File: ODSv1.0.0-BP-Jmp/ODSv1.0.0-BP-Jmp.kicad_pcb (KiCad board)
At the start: 2 copper layers, 150 x 150 mm, 73 parts, among them J1 Conn_01x16, J10 Conn_02x10_Odd_Even, J11 Conn_02x10_Odd_Even, J12 Conn_02x10_Odd_Even, J13 Conn_02x10_Odd_Even, J14 Conn_02x10_Odd_Even, J15 Conn_02x10_Odd_Even, J16 Conn_02x10_Odd_Even, J17 Conn_02x10_Odd_Even, J18 Conn_02x10_Odd_Even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

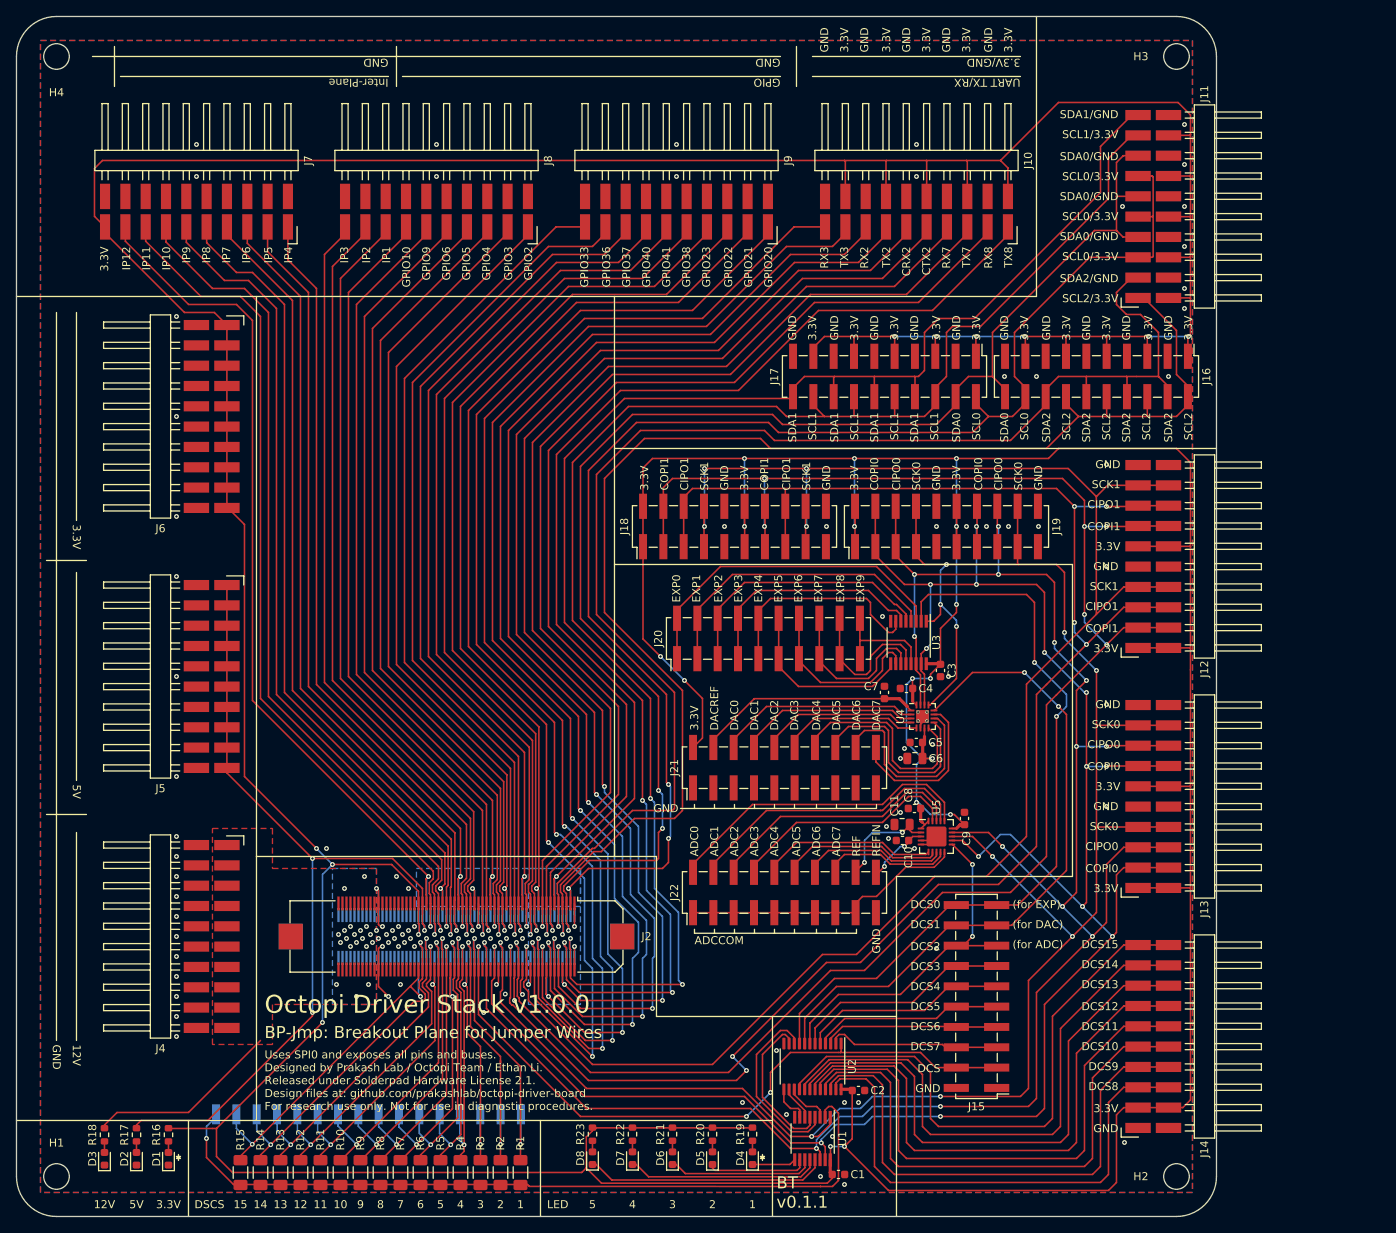
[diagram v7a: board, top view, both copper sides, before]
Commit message: Add silkscreen labels showing BP-Jmp's various sections
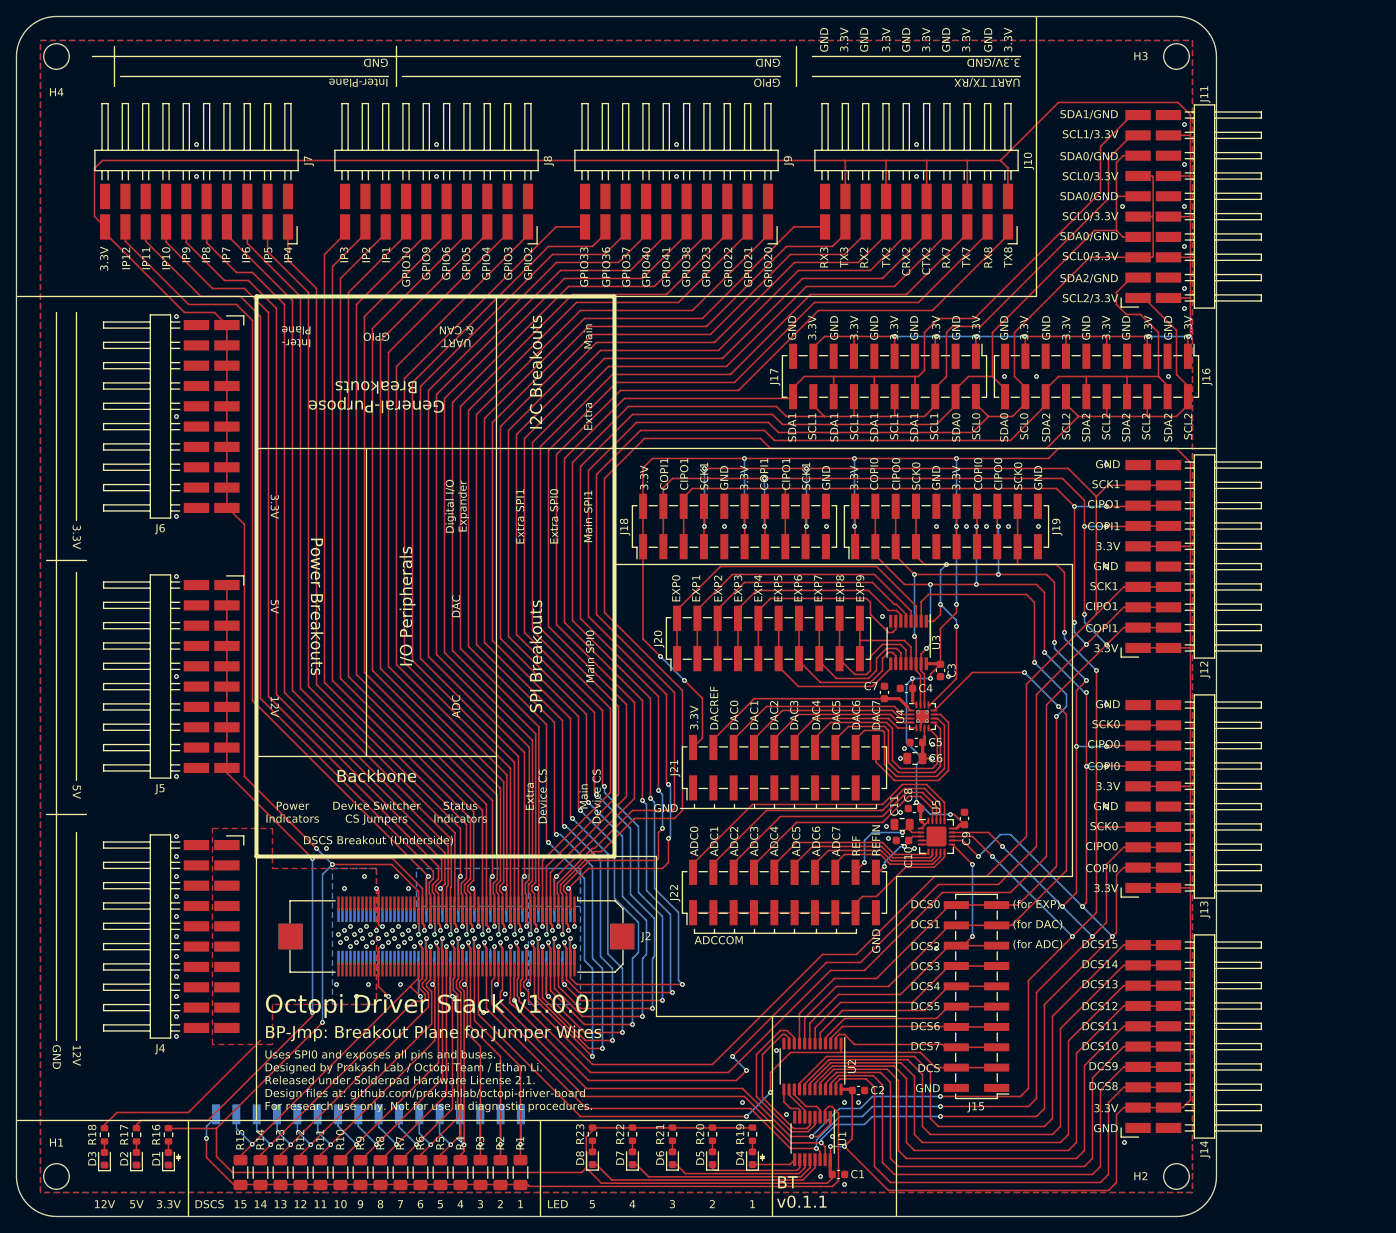
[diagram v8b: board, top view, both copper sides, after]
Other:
- board text added: "ADC"
- board text added: "Backbone"
- board text added: "DAC"
- board text added: "DSCS Breakout (Underside)"
- board text added: "Device Switcher CS Jumpers"
- board text added: "Digital I/O Expander"
- board text added: "Extra"
- board text added: "Extra Device CS"
- board text added: "Extra SPI0"
- board text added: "Extra SPI1"
- board text added: "General-Purpose Breakouts"
- board text added: "I/O Peripherals"
- board text added: "I2C Breakouts"
- board text added: "Inter- Plane"
- board text added: "Main"
- board text added: "Main Device CS"
- board text added: "Main SPI0"
- board text added: "Main SPI1"
- board text added: "Power Breakouts"
- board text added: "Power Indicators"
- board text added: "SPI Breakouts"
- board text added: "Status Indicators"
- board text added: "UART & CAN"
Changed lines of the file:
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@@
   (general
     (thickness 1.6)
-    (drawings 342)
+    (drawings 375)
     (tracks 2545)
     (zones 0)
@@
   )
   (layers
-    (0 F.Cu signal)
-    (31 B.Cu signal)
+    (0 F.Cu signal hide)
+    (31 B.Cu signal hide)
     (32 B.Adhes user)
     (33 F.Adhes user)
@@
     )
   )
+  (gr_text "DSCS Breakout (Underside)" (at 75.25 163) (layer F.SilkS)
+    (effects (font (size 1 1) (thickness 0.15)))
+  )
+  (gr_text "Extra\nDevice CS" (at 95 157.5 90) (layer F.SilkS)
+    (effects (font (size 1 1) (thickness 0.15)))
+  )
+  (gr_text "Main\nDevice CS" (at 101.75 157.5 90) (layer F.SilkS)
+    (effects (font (size 1 1) (thickness 0.15)))
+  )
+  (gr_line (start 30 95) (end 60 95) (layer F.SilkS) (width 0.12))
+  (gr_line (start 60 95) (end 104.75 95) (layer F.SilkS) (width 0.5))
+  (gr_line (start 60 95) (end 60 165) (layer F.SilkS) (width 0.5))
+  (gr_line (start 60 165) (end 104.75 165) (layer F.SilkS) (width 0.5))
+  (gr_text "Extra SPI1" (at 93 122.5 90) (layer F.SilkS)
+    (effects (font (size 1 1) (thickness 0.15)))
+  )
+  (gr_text "Extra SPI0" (at 97.25 122.5 90) (layer F.SilkS)
+    (effects (font (size 1 1) (thickness 0.15)))
+  )
+  (gr_text "Main SPI0" (at 101.75 140 90) (layer F.SilkS)
+    (effects (font (size 1 1) (thickness 0.15)))
+  )
+  (gr_text "Main SPI1" (at 101.5 122.5 90) (layer F.SilkS)
+    (effects (font (size 1 1) (thickness 0.15)))
+  )
+  (gr_text Extra (at 101.5 110 90) (layer F.SilkS)
+    (effects (font (size 1 1) (thickness 0.15)))
+  )
+  (gr_text Main (at 101.5 100 90) (layer F.SilkS)
+    (effects (font (size 1 1) (thickness 0.15)))
+  )
+  (gr_text ADC (at 85 146.25 90) (layer F.SilkS)
+    (effects (font (size 1 1) (thickness 0.15)))
+  )
+  (gr_text DAC (at 85 133.75 90) (layer F.SilkS)
+    (effects (font (size 1 1) (thickness 0.15)))
+  )
+  (gr_text "Digital I/O\nExpander" (at 85 121.25 90) (layer F.SilkS)
+    (effects (font (size 1 1) (thickness 0.15)))
+  )
+  (gr_line (start 73.75 152.5) (end 73.75 114) (layer F.SilkS) (width 0.12))
+  (gr_line (start 90 152.5) (end 60 152.5) (layer F.SilkS) (width 0.12))
+  (gr_line (start 90 165) (end 90 95) (layer F.SilkS) (width 0.12))
+  (gr_text "UART\n& CAN" (at 85 100 180) (layer F.SilkS)
+    (effects (font (size 1 1) (thickness 0.15)))
+  )
+  (gr_text GPIO (at 75 100 180) (layer F.SilkS)
+    (effects (font (size 1 1) (thickness 0.15)))
+  )
+  (gr_text "Inter-\nPlane" (at 65 100 180) (layer F.SilkS)
+    (effects (font (size 1 1) (thickness 0.15)))
+  )
+  (gr_text 12V (at 62.25 146.25 -90) (layer F.SilkS)
+    (effects (font (size 1 1) (thickness 0.15)))
+  )
+  (gr_text 5V (at 62.25 133.75 -90) (layer F.SilkS)
+    (effects (font (size 1 1) (thickness 0.15)))
+  )
+  (gr_text 3.3V (at 62.25 121.25 -90) (layer F.SilkS)
+    (effects (font (size 1 1) (thickness 0.15)))
+  )
+  (gr_text Backbone (at 75 155) (layer F.SilkS)
+    (effects (font (size 1.5 1.5) (thickness 0.3)))
+  )
+  (gr_text "I/O Peripherals" (at 78.75 133.75 90) (layer F.SilkS)
+    (effects (font (size 1.5 1.5) (thickness 0.3)))
+  )
+  (gr_text "SPI Breakouts" (at 95 140 90) (layer F.SilkS)
+    (effects (font (size 1.5 1.5) (thickness 0.3)))
+  )
+  (gr_text "I2C Breakouts" (at 95 104.5 90) (layer F.SilkS)
+    (effects (font (size 1.5 1.5) (thickness 0.3)))
+  )
+  (gr_text "General-Purpose\nBreakouts" (at 75 107.5 180) (layer F.SilkS)
+    (effects (font (size 1.5 1.5) (thickness 0.3)))
+  )
+  (gr_text "Power Breakouts" (at 67.5 133.75 -90) (layer F.SilkS)
+    (effects (font (size 1.5 1.5) (thickness 0.3)))
+  )
+  (gr_text "Status\nIndicators" (at 85.5 159.5) (layer F.SilkS)
+    (effects (font (size 1 1) (thickness 0.15)))
+  )
+  (gr_text "Device Switcher\nCS Jumpers" (at 75 159.5) (layer F.SilkS)
+    (effects (font (size 1 1) (thickness 0.15)))
+  )
+  (gr_text "Power\nIndicators" (at 64.5 159.5) (layer F.SilkS)
+    (effects (font (size 1 1) (thickness 0.15)))
+  )
   (gr_line (start 124.5 185) (end 124.5 210) (layer F.SilkS) (width 0.12))
   (gr_line (start 117.25 174.1) (end 117.25 174.6) (layer F.SilkS) (width 0.15))
@@
   (gr_line (start 162 167.5) (end 162 128.5) (layer F.SilkS) (width 0.12))
   (gr_line (start 162 128.5) (end 104.75 128.5) (layer F.SilkS) (width 0.12))
-  (gr_line (start 104.75 165) (end 104.75 95) (layer F.SilkS) (width 0.12))
+  (gr_line (start 104.75 165) (end 104.75 95) (layer F.SilkS) (width 0.5))
   (gr_text SCK1 (at 128.75 119.25 90) (layer F.SilkS)
     (effects (font (size 1 1) (thickness 0.15)) (justify left))
@@
     (effects (font (size 1 1) (thickness 0.15)) (justify left))
   )
-  (gr_line (start 180 114) (end 104.75 114) (layer F.SilkS) (width 0.12))
+  (gr_line (start 180 114) (end 60 114) (layer F.SilkS) (width 0.12))
   (gr_text SDA1 (at 127 109.5 90) (layer F.SilkS)
     (effects (font (size 1 1) (thickness 0.15)) (justify right))
@@
   )
   (gr_line (start 37.5 129.5) (end 37.5 155.5) (layer F.SilkS) (width 0.12))
-  (gr_line (start 30 95) (end 157.5 95) (layer F.SilkS) (width 0.12))
+  (gr_line (start 104.75 95) (end 157.5 95) (layer F.SilkS) (width 0.12))
   (gr_text GND (at 35 188.5 -90) (layer F.SilkS)
     (effects (font (size 1 1) (thickness 0.15)) (justify left))
@@
     (effects (font (size 1 1) (thickness 0.15)) (justify left))
   )
-  (gr_line (start 60 95) (end 60 165) (layer F.SilkS) (width 0.12))
   (gr_line (start 140 167.5) (end 162 167.5) (layer F.SilkS) (width 0.12))
   (gr_text "BP-Jmp: Breakout Plane for Jumper Wires" (at 61 187) (layer F.SilkS)
@@
     (effects (font (size 1.5 1.5) (thickness 0.3)) (justify left))
   )
-  (gr_line (start 60 165) (end 110 165) (layer F.SilkS) (width 0.12))
+  (gr_line (start 104.75 165) (end 110 165) (layer F.SilkS) (width 0.12))
   (gr_text 5 (at 102 208.5) (layer F.SilkS)
     (effects (font (size 1 1) (thickness 0.15)))
